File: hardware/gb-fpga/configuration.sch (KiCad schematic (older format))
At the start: 2 parts, among them U1 xc7s25ftgb196

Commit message: Add GND net
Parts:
- removed U?: MX25L3233F, Package_SO:SOP-8_3.9x4.9mm_P1.27mm, symbol Memory_Flash:MX25L3233F
- added U2: MX25R3235FZNxx1, Package_SON:WSON-8-1EP_6x5mm_P1.27mm_EP3.4x4mm, symbol Memory_Flash:MX25R3235FZNxx1
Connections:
- net labels added: GND
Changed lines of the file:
@@
-	1    0    0    -1
-$EndComp
-$Comp
-L Memory_Flash:MX25L3233F U?
-U 1 1 60D202EC
-P 4200 3250
-F 0 "U?" H 4744 3296 50  0000 L CNN
-F 1 "MX25L3233F" H 4744 3205 50  0000 L CNN
-F 2 "Package_SO:SOP-8_3.9x4.9mm_P1.27mm" H 4200 2650 50  0001 C CNN
-F 3 "http://www.macronix.com/Lists/Datasheet/Attachments/7534/MX25R3235F,%20Wide%20Range,%2032Mb,%20v1.6.pdf" H 4200 3250 50  0001 C CNN
-	1    4200 3250
 	1    0    0    -1
 $EndComp
@@
 Wire Wire Line
 	3200 3150 3700 3150
+$Comp
+L power:GND #PWR0101
+U 1 1 60D22A7C
+P 4400 3650
+F 0 "#PWR0101" H 4400 3400 50  0001 C CNN
+F 1 "GND" H 4405 3477 50  0000 C CNN
+F 2 "" H 4400 3650 50  0001 C CNN
+F 3 "" H 4400 3650 50  0001 C CNN
+	1    4400 3650
+	1    0    0    -1
+$EndComp
+$Comp
+L Memory_Flash:MX25R3235FZNxx1 U2
+U 1 1 60D24FDA
+P 4200 3250
+F 0 "U2" H 4744 3296 50  0000 L CNN
+F 1 "MX25R3235FZNxx1" H 4744 3205 50  0000 L CNN
+F 2 "Package_SON:WSON-8-1EP_6x5mm_P1.27mm_EP3.4x4mm" H 4200 2650 50  0001 C CNN
+F 3 "http://www.macronix.com/Lists/Datasheet/Attachments/7534/MX25R3235F,%20Wide%20Range,%2032Mb,%20v1.6.pdf" H 4200 3250 50  0001 C CNN
+	1    4200 3250
+	1    0    0    -1
+$EndComp
 $EndSCHEMATC

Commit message: Use USON footprint for flash memory
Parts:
- removed U2: MX25R3235FZNxx1, Package_SON:WSON-8-1EP_6x5mm_P1.27mm_EP3.4x4mm, symbol Memory_Flash:MX25R3235FZNxx1
- added U2: MX25R3235FZBxx1, Package_SON:USON-8_4.0x3.0mm_P0.8mm, symbol Memory_Flash:MX25R3235FZBxx1
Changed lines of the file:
@@
 $EndComp
 $Comp
-L Memory_Flash:MX25R3235FZNxx1 U2
-U 1 1 60D24FDA
+L Memory_Flash:MX25R3235FZBxx1 U2
+U 1 1 60D29283
 P 4200 3250
 F 0 "U2" H 4744 3296 50  0000 L CNN
-F 1 "MX25R3235FZNxx1" H 4744 3205 50  0000 L CNN
-F 2 "Package_SON:WSON-8-1EP_6x5mm_P1.27mm_EP3.4x4mm" H 4200 2650 50  0001 C CNN
+F 1 "MX25R3235FZBxx1" H 4744 3205 50  0000 L CNN
+F 2 "Package_SON:USON-8_4.0x3.0mm_P0.8mm" H 4200 2650 50  0001 C CNN
 F 3 "http://www.macronix.com/Lists/Datasheet/Attachments/7534/MX25R3235F,%20Wide%20Range,%2032Mb,%20v1.6.pdf" H 4200 3250 50  0001 C CNN
 	1    4200 3250

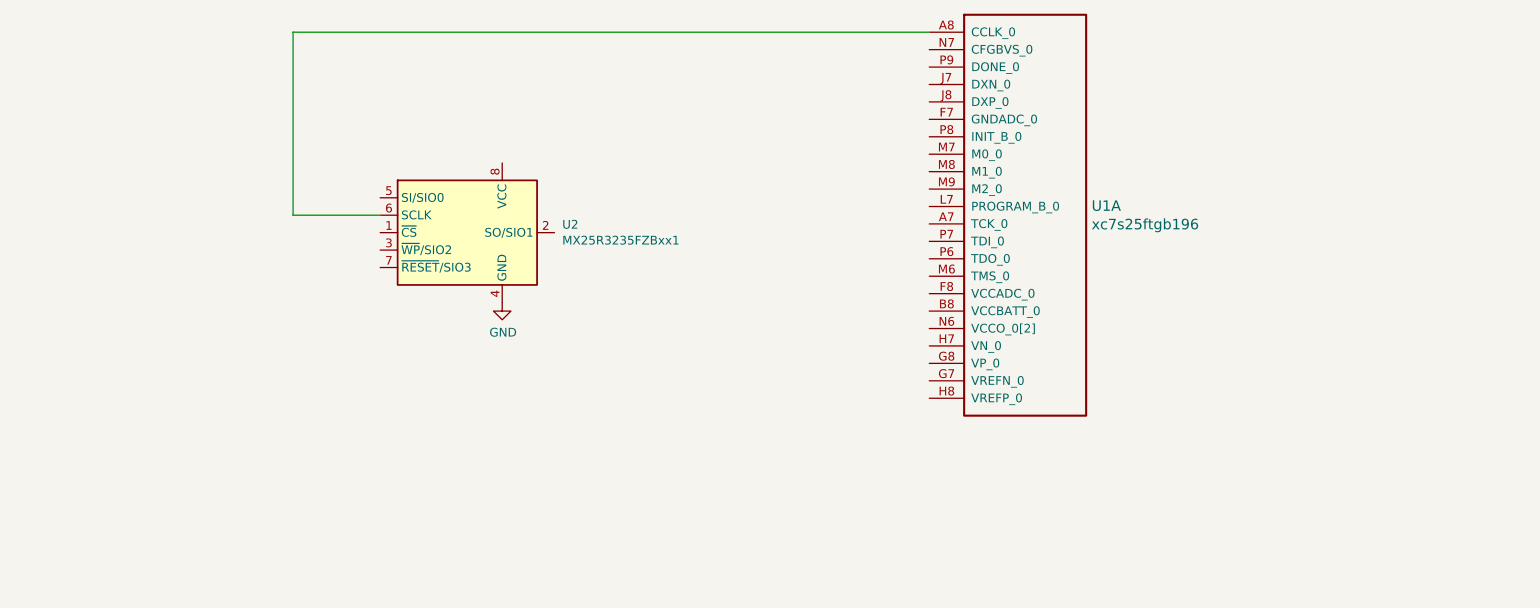
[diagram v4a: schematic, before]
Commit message: Add connections to flash ic
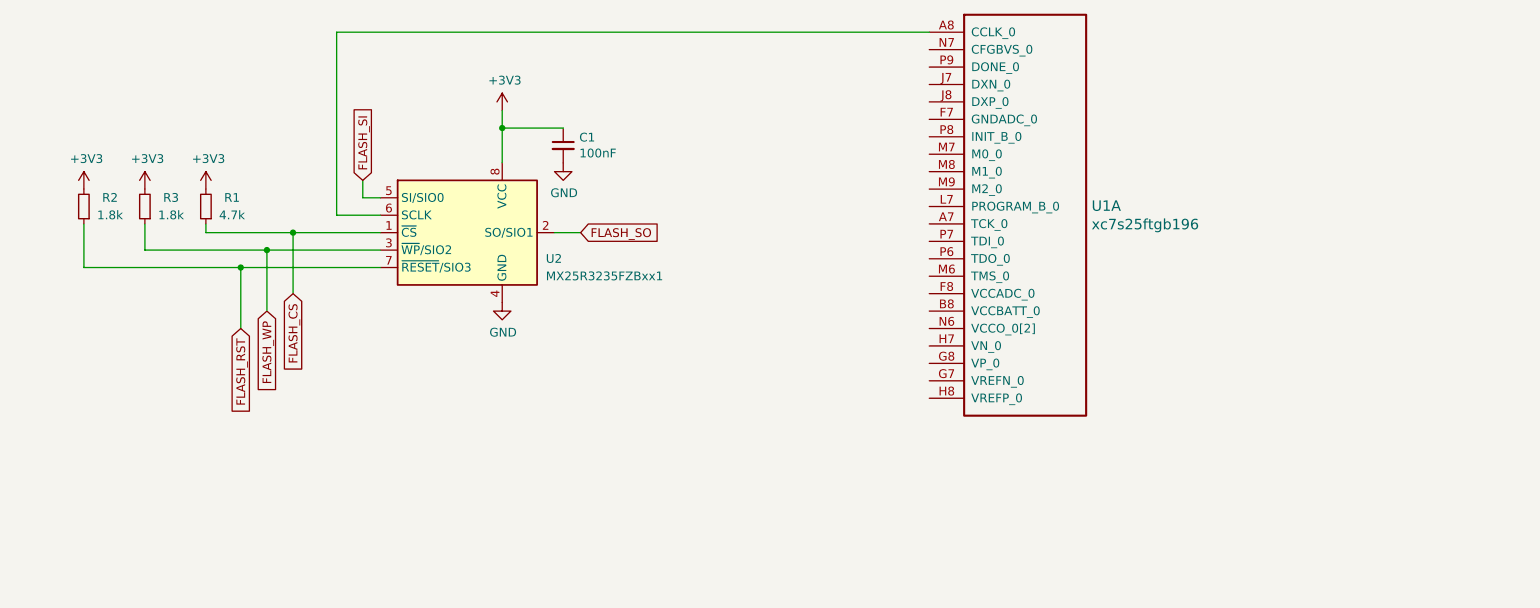
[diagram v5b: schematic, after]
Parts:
- added C1: 100nF, Capacitor_SMD:C_0603_1608Metric, symbol Device:C_Small
- added R1: 4.7k, Resistor_SMD:R_0603_1608Metric, symbol Device:R_Small
- added R2, R3: 1.8k, Resistor_SMD:R_0603_1608Metric, symbol Device:R_Small
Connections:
- net GND: now also C1.2
- net FLASH_CS: now reaches U2.1 (~CS)
- net FLASH_CS: now also R1.1
- net FLASH_SO: now reaches U2.2 (SO/SIO1)
- net FLASH_WP: now reaches U2.3 (~WP~/SIO2)
- net FLASH_WP: now also R3.1
- net FLASH_SI: now reaches U2.5 (SI/SIO0)
- net FLASH_RST: now reaches U2.7 (~RESET~/SIO3)
- net FLASH_RST: now also R2.1
- net +3V3: now reaches U2.8 (VCC)
- net +3V3: now also C1.1, R1.2, R2.2, R3.2
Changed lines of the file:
@@
 $EndComp
 Wire Wire Line
-	6850 2100 3200 2100
+	6850 2100 3450 2100
 Wire Wire Line
-	3200 2100 3200 3150
+	3450 2100 3450 3150
 Wire Wire Line
-	3200 3150 3700 3150
+	3450 3150 3700 3150
 $Comp
 L power:GND #PWR0101
@@
 $EndComp
 $Comp
+L power:+3V3 #PWR0106
+U 1 1 60D44063
+P 4400 2550
+F 0 "#PWR0106" H 4400 2400 50  0001 C CNN
+F 1 "+3V3" H 4415 2723 50  0000 C CNN
+F 2 "" H 4400 2550 50  0001 C CNN
+F 3 "" H 4400 2550 50  0001 C CNN
+	1    4400 2550
+	1    0    0    -1
+$EndComp
+Wire Wire Line
+	4400 2550 4400 2650
+$Comp
+L Device:C_Small C1
+U 1 1 60D4671F
+P 4750 2750
+F 0 "C1" H 4842 2796 50  0000 L CNN
+F 1 "100nF" H 4842 2705 50  0000 L CNN
+F 2 "Capacitor_SMD:C_0603_1608Metric" H 4750 2750 50  0001 C CNN
+F 3 "~" H 4750 2750 50  0001 C CNN
+	1    4750 2750
+	1    0    0    -1
+$EndComp
+$Comp
+L power:GND #PWR0107
+U 1 1 60D480A1
+P 4750 2850
+F 0 "#PWR0107" H 4750 2600 50  0001 C CNN
+F 1 "GND" H 4755 2677 50  0000 C CNN
+F 2 "" H 4750 2850 50  0001 C CNN
+F 3 "" H 4750 2850 50  0001 C CNN
+	1    4750 2850
+	1    0    0    -1
+$EndComp
+Wire Wire Line
+	4750 2650 4400 2650
+Connection ~ 4400 2650
+Wire Wire Line
+	4400 2650 4400 2850
+$Comp
+L Device:R_Small R1
+U 1 1 60D4AB05
+P 2700 3100
+F 0 "R1" H 2550 3050 50  0000 C CNN
+F 1 "4.7k" H 2550 3150 50  0000 C CNN
+F 2 "Resistor_SMD:R_0603_1608Metric" H 2700 3100 50  0001 C CNN
+F 3 "~" H 2700 3100 50  0001 C CNN
+	1    2700 3100
+	-1   0    0    1
+$EndComp
+$Comp
+L power:+3V3 #PWR0108
+U 1 1 60D4BCCC
+P 2700 3000
+F 0 "#PWR0108" H 2700 2850 50  0001 C CNN
+F 1 "+3V3" H 2715 3173 50  0000 C CNN
+F 2 "" H 2700 3000 50  0001 C CNN
+F 3 "" H 2700 3000 50  0001 C CNN
+	1    2700 3000
+	1    0    0    -1
+$EndComp
+Wire Wire Line
+	3700 3250 3200 3250
+$Comp
 L Memory_Flash:MX25R3235FZBxx1 U2
-U 1 1 60D29283
+U 1 1 60D4EC7E
 P 4200 3250
-F 0 "U2" H 4744 3296 50  0000 L CNN
-F 1 "MX25R3235FZBxx1" H 4744 3205 50  0000 L CNN
+F 0 "U2" H 4650 3100 50  0000 L CNN
+F 1 "MX25R3235FZBxx1" H 4650 3000 50  0000 L CNN
 F 2 "Package_SON:USON-8_4.0x3.0mm_P0.8mm" H 4200 2650 50  0001 C CNN
 F 3 "http://www.macronix.com/Lists/Datasheet/Attachments/7534/MX25R3235F,%20Wide%20Range,%2032Mb,%20v1.6.pdf" H 4200 3250 50  0001 C CNN
@@
 	1    0    0    -1
 $EndComp
+Wire Wire Line
+	2700 3250 2700 3200
+$Comp
+L Device:R_Small R3
+U 1 1 60D5B55D
+P 2350 3100
+F 0 "R3" H 2200 3050 50  0000 C CNN
+F 1 "1.8k" H 2200 3150 50  0000 C CNN
+F 2 "Resistor_SMD:R_0603_1608Metric" H 2350 3100 50  0001 C CNN
+F 3 "~" H 2350 3100 50  0001 C CNN
+	1    2350 3100
+	-1   0    0    1
+$EndComp
+$Comp
+L Device:R_Small R2
+U 1 1 60D5BFAC
+P 2000 3100
+F 0 "R2" H 1850 3050 50  0000 C CNN
+F 1 "1.8k" H 1850 3150 50  0000 C CNN
+F 2 "Resistor_SMD:R_0603_1608Metric" H 2000 3100 50  0001 C CNN
+F 3 "~" H 2000 3100 50  0001 C CNN
+	1    2000 3100
+	-1   0    0    1
+$EndComp
+$Comp
+L power:+3V3 #PWR0109
+U 1 1 60D5C464
+P 2350 3000
+F 0 "#PWR0109" H 2350 2850 50  0001 C CNN
+F 1 "+3V3" H 2365 3173 50  0000 C CNN
+F 2 "" H 2350 3000 50  0001 C CNN
+F 3 "" H 2350 3000 50  0001 C CNN
+	1    2350 3000
+	1    0    0    -1
+$EndComp
+$Comp
+L power:+3V3 #PWR0110
+U 1 1 60D5D2AC
+P 2000 3000
+F 0 "#PWR0110" H 2000 2850 50  0001 C CNN
+F 1 "+3V3" H 2015 3173 50  0000 C CNN
+F 2 "" H 2000 3000 50  0001 C CNN
+F 3 "" H 2000 3000 50  0001 C CNN
+	1    2000 3000
+	1    0    0    -1
+$EndComp
+Wire Wire Line
+	3700 3350 3050 3350
+Wire Wire Line
+	2350 3350 2350 3200
+Wire Wire Line
+	3700 3450 2900 3450
+Wire Wire Line
+	2000 3450 2000 3200
+Wire Wire Line
+	3200 3250 3200 3600
+Connection ~ 3200 3250
+Wire Wire Line
+	3200 3250 2700 3250
+Wire Wire Line
+	3050 3350 3050 3700
+Connection ~ 3050 3350
+Wire Wire Line
+	3050 3350 2350 3350
+Wire Wire Line
+	2900 3450 2900 3800
+Connection ~ 2900 3450
+Wire Wire Line
+	2900 3450 2000 3450
+Text GLabel 3200 3600 3    50   Input ~ 0
+FLASH_CS
+Text GLabel 3050 3700 3    50   Input ~ 0
+FLASH_WP
+Text GLabel 2900 3800 3    50   Input ~ 0
+FLASH_RST
+Wire Wire Line
+	4700 3250 4850 3250
+Wire Wire Line
+	3700 3050 3600 3050
+Wire Wire Line
+	3600 3050 3600 2950
+Text GLabel 4850 3250 2    50   Input ~ 0
+FLASH_SO
+Text GLabel 3600 2950 1    50   Input ~ 0
+FLASH_SI
 $EndSCHEMATC

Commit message: Connect flash config circuit
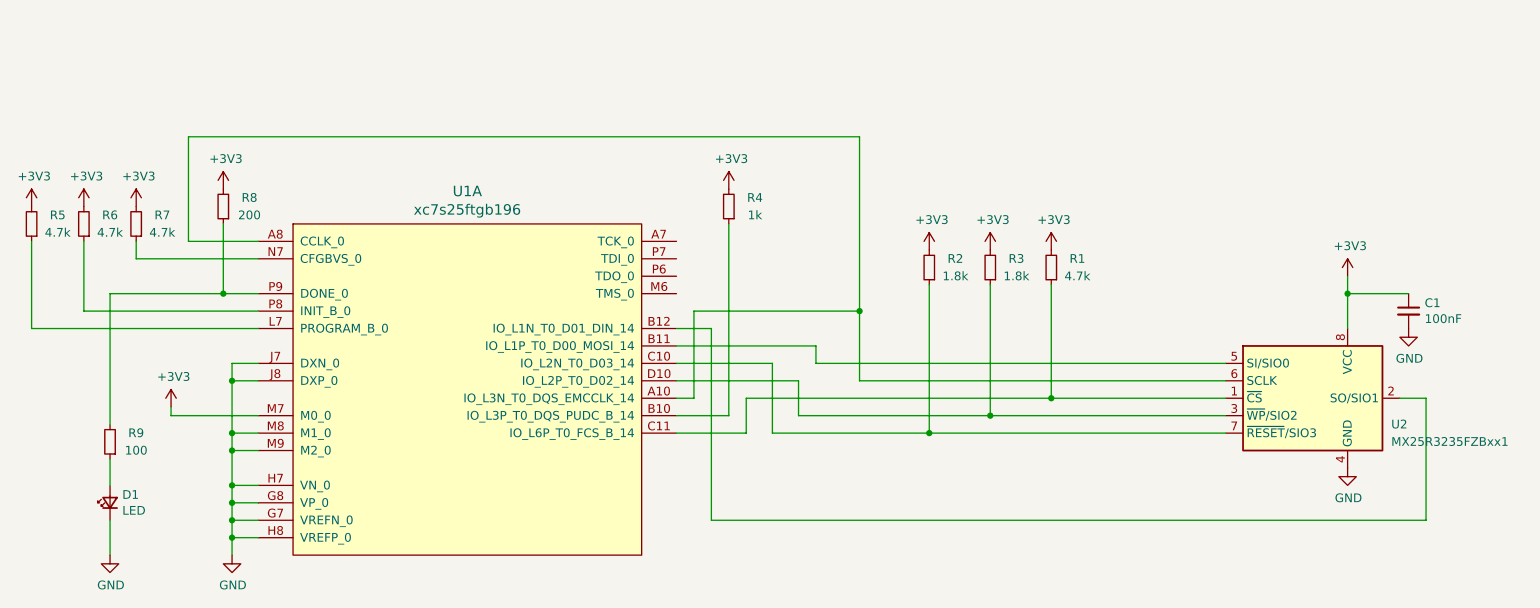
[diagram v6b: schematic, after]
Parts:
- removed U1: xc7s25ftgb196, Package_BGA:Xilinx_FTGB196, symbol xilinx7:xc7s25ftgb196
- added D1: LED, LED_SMD:LED_0603_1608Metric, symbol Device:LED_Small
- added R4: 1k, Resistor_SMD:R_0603_1608Metric, symbol Device:R_Small
- added R5, R6, R7: 4.7k, Resistor_SMD:R_0603_1608Metric, symbol Device:R_Small
- added R8: 200, Resistor_SMD:R_0603_1608Metric, symbol Device:R_Small
- added R9: 100, Resistor_SMD:R_0603_1608Metric, symbol Device:R_Small
- added U1: xc7s25ftgb196, symbol gb-fpga:xc7s25ftgb196
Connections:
- net +3V3: now also R4.2, R5.2, R6.2, R7.2, R8.2, U1.M7 (M0_0)
- net GND: now also D1.1 (K), U1.G7 (VREFN_0), U1.G8 (VP_0), U1.H7 (VN_0), U1.H8 (VREFP_0), U1.J7 (DXN_0), U1.J8 (DXP_0), U1.M8 (M1_0), U1.M9 (M2_0)
- net at U2.6 (SCLK): now also U1.A10 (IO_L3N_T0_DQS_EMCCLK_14), U1.A8 (CCLK_0)
- net FLASH_CS: no longer names the net of R1.1, U2.1 (~CS)
- net FLASH_CS: now also U1.C11 (IO_L6P_T0_FCS_B_14)
- net FLASH_RST: no longer names the net of R2.1, U2.7 (~RESET~/SIO3)
- net FLASH_RST: now also U1.C10 (IO_L2N_T0_D03_14)
- net FLASH_SI: no longer names the net of U2.5 (SI/SIO0)
- net FLASH_SI: now also U1.B11 (IO_L1P_T0_D00_MOSI_14)
- net FLASH_SO: no longer names the net of U2.2 (SO/SIO1)
- net FLASH_SO: now also U1.B12 (IO_L1N_T0_D01_DIN_14)
- net FLASH_WP: no longer names the net of R3.1, U2.3 (~WP~/SIO2)
- net FLASH_WP: now also U1.D10 (IO_L2P_T0_D02_14)
- new net: R4.1, U1.B10 (IO_L3P_T0_DQS_PUDC_B_14)
- new net: R5.1, U1.L7 (PROGRAM_B_0)
- new net: R7.1, U1.N7 (CFGBVS_0)
- new net: R6.1, U1.P8 (INIT_B_0)
- new net: R8.1, R9.2, U1.P9 (DONE_0)
- new net: D1.2 (A), R9.1
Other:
- moved on the sheet: C1, R1, R2, R3, U2

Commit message: Add USB connections
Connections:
- net TCK: now reaches U1.A7 (TCK_0)
- net TMS: now reaches U1.M6 (TMS_0)
- net TDO: now reaches U1.P6 (TDO_0)
- net TDI: now reaches U1.P7 (TDI_0)
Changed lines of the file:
@@
 	5400 4300 5700 4300
-Wire Wire Line
-	5700 4300 5700 3200
-$Comp
-L Device:R_Small R4
-U 1 1 60DA54B4
-P 5700 3100
-F 0 "R4" H 5550 3050 50  0000 C CNN
-F 1 "1k" H 5550 3150 50  0000 C CNN
-F 2 "Resistor_SMD:R_0603_1608Metric" H 5700 3100 50  0001 C CNN
-F 3 "~" H 5700 3100 50  0001 C CNN
-	1    5700 3100
-	-1   0    0    1
-$EndComp
-$Comp
-L power:+3V3 #PWR0111
-U 1 1 60DA5CD7
-P 5700 3000
-F 0 "#PWR0111" H 5700 2850 50  0001 C CNN
-F 1 "+3V3" H 5715 3173 50  0000 C CNN
-F 2 "" H 5700 3000 50  0001 C CNN
-F 3 "" H 5700 3000 50  0001 C CNN
-	1    5700 3000
-	1    0    0    -1
-$EndComp
 Wire Wire Line
 	3000 3400 2300 3400
@@
 Wire Wire Line
 	2150 5100 2150 4900
+$Comp
+L power:+3V3 #PWR0111
+U 1 1 60DA5CD7
+P 5700 3000
+F 0 "#PWR0111" H 5700 2850 50  0001 C CNN
+F 1 "+3V3" H 5715 3173 50  0000 C CNN
+F 2 "" H 5700 3000 50  0001 C CNN
+F 3 "" H 5700 3000 50  0001 C CNN
+	1    5700 3000
+	1    0    0    -1
+$EndComp
+Wire Wire Line
+	5700 4300 5700 3200
+$Comp
+L Device:R_Small R4
+U 1 1 60DA54B4
+P 5700 3100
+F 0 "R4" H 5550 3050 50  0000 C CNN
+F 1 "1k" H 5550 3150 50  0000 C CNN
+F 2 "Resistor_SMD:R_0603_1608Metric" H 5700 3100 50  0001 C CNN
+F 3 "~" H 5700 3100 50  0001 C CNN
+	1    5700 3100
+	-1   0    0    1
+$EndComp
+Wire Wire Line
+	5400 3300 5850 3300
+Wire Wire Line
+	5400 3400 5850 3400
+Wire Wire Line
+	5400 3500 5850 3500
+Wire Wire Line
+	5400 3600 5850 3600
+Text GLabel 5850 3300 2    50   Input ~ 0
+TCK
+Text GLabel 5850 3400 2    50   Input ~ 0
+TDI
+Text GLabel 5850 3500 2    50   Output ~ 0
+TDO
+Text GLabel 5850 3600 2    50   Input ~ 0
+TMS
 $EndSCHEMATC
